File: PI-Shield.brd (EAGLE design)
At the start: 69.8 x 73 mm, 77 parts, among them IC1 PCF8574T, J10 T2I, J11 T2I, J12 T2I, J13 DF13-4P-1.25DSA, J14 DF13-4P-1.25DSA, J15 DF13-4P-1.25DSA, Q1 220mA/50V/3.5Ω, Q2 220mA/50V/3.5Ω, Q3 220mA/50V/3.5Ω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

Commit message: Update PI-Shield.brd
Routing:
- net 5V: track 177.8 -> 182.7 mm, vias 4 -> 5
- net 5V_RAW: track 2.52 -> 6.33 mm
- net SCL: track 141.0 -> 139.3 mm
- net SDA: track 141.7 -> 140.1 mm
- net PI_POWER: track 28.4 -> 30.0 mm
- net SOL6_1: track 47.8 -> 49.2 mm
- net SOL5_1: track 42.0 -> 43.1 mm
- net RESET_MID: track 12.5 -> 13.7 mm
- net SOL4_1: track 37.3 -> 38.3 mm
- net SOL3_1: track 31.8 -> 32.7 mm
- net 3V3: track 219.9 -> 220.7 mm
- net SOL2_1: track 26.9 -> 27.5 mm

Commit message: Added CAN to BKP... Silkscreen as well
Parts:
- removed U$3: 6X_CONN, PI-SHIELD, Solenoid-Backplane:IPL6X2
- added U$9: 7X_CONN, PI-SHIELD, Solenoid-Backplane:IPL7X2
- moved U$6 1.02 mm to (36.7, 5.46)
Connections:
- net 12V: now also U$9.2, U$9.4; no longer U$3.2, U$3.4
- net 3V3: now also U$9.12; no longer U$3.12
- net 5V: now also U$9.8; no longer U$3.8
- net CAN_H: now also U$9.13
- net CAN_L: now also U$9.14
- net GND: now also U$9.10, U$9.6; no longer U$3.10, U$3.6
- net SOL1_1: now also U$9.1; no longer U$3.1
- net SOL2_1: now also U$9.3; no longer U$3.3
- net SOL3_1: now also U$9.5; no longer U$3.5
- net SOL4_1: now also U$9.7; no longer U$3.7
- net SOL5_1: now also U$9.9; no longer U$3.9
- net SOL6_1: now also U$9.11; no longer U$3.11
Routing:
- net CAN_L: track 43.0 -> 137.5 mm, vias 1 -> 2
- net CAN_H: track 43.0 -> 136.6 mm, vias 1 -> 2
- net !AMP_RESET: track 55.6 -> 51.8 mm
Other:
- board text added: "X14 Pi-Shield v1 Rachel Livesay Erin Park Katherine Sandys Read Hedl 1/7/2022"

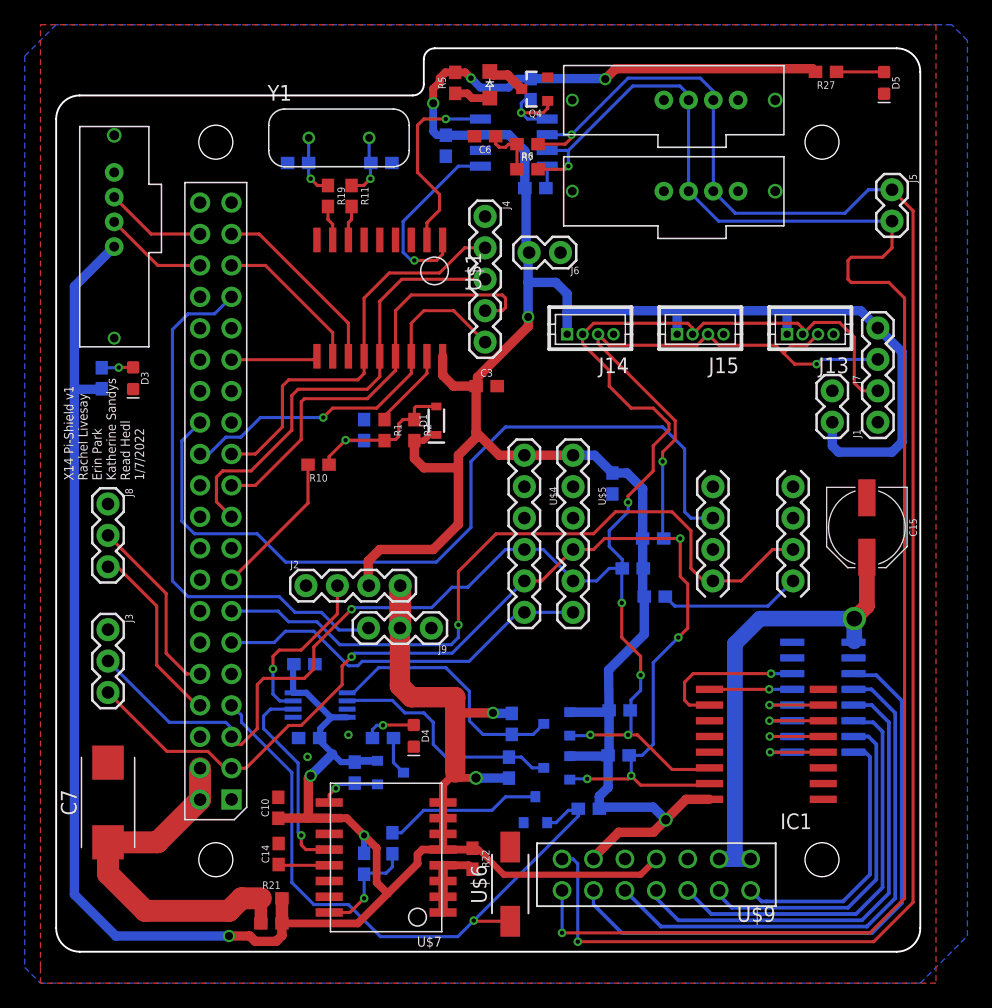
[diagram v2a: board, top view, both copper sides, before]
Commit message: Adjusted Labels
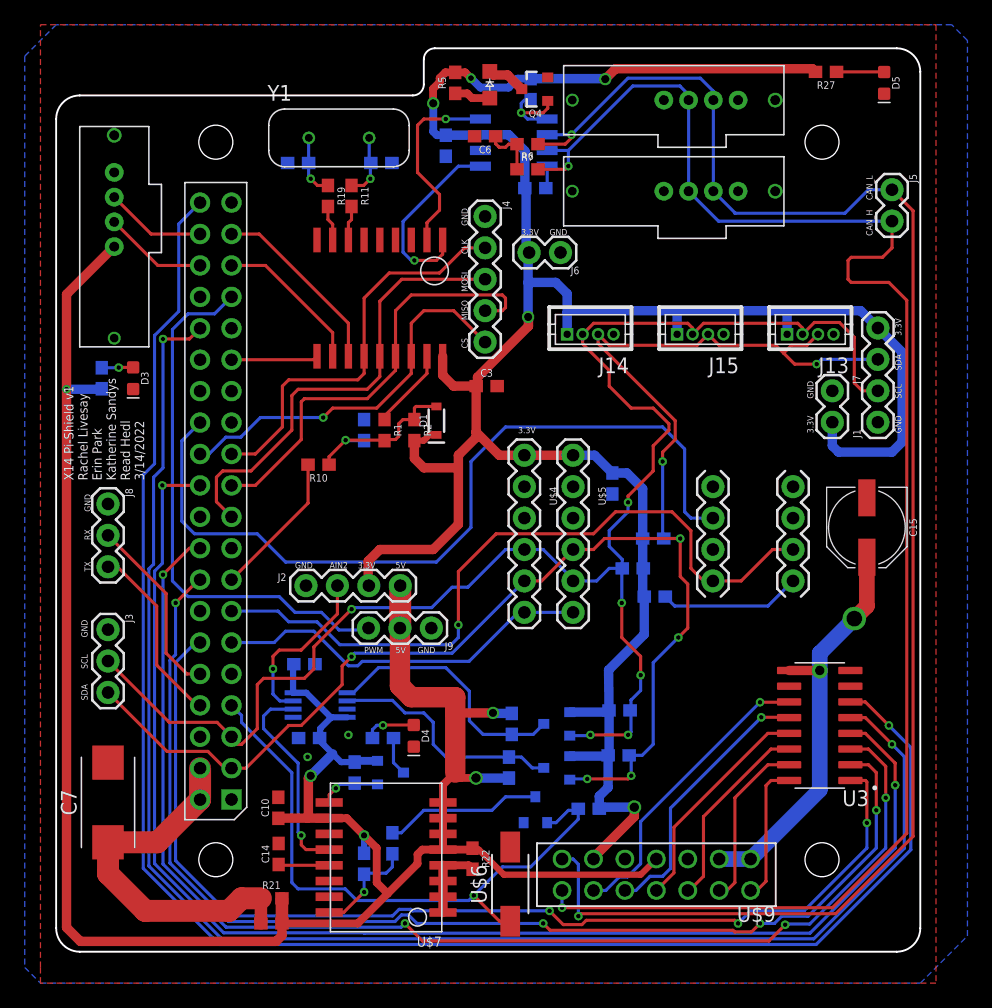
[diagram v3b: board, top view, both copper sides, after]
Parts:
- removed IC1: PCF8574T, micro-philips:SO16W
- moved U3 2.30 mm to (61.7, 18.3), flipped to the top
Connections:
- net 3V3: no longer IC1.16
- net GND: no longer IC1.1, IC1.2, IC1.3, IC1.8
- net GPIO1: now also U$8.12; no longer IC1.4
- net GPIO2: now also U$8.16; no longer IC1.5
- net GPIO3: now also U$8.18; no longer IC1.6
- net GPIO4: now also U$8.22; no longer IC1.7
- net GPIO5: now also U$8.32; no longer IC1.9
- net GPIO6: now also U$8.40; no longer IC1.10
- net SCL: no longer IC1.14
- net SDA: no longer IC1.15
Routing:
- net GPIO6: track 12.6 -> 138.2 mm
- net GPIO5: track 6.70 -> 126.0 mm, vias 1 -> 2
- net GPIO4: track 6.19 -> 110.4 mm, vias 1 -> 2
- net GPIO3: track 6.19 -> 101.7 mm, vias 1 -> 4
- net GPIO2: track 6.14 -> 95.1 mm, vias 1 -> 4
- net GPIO1: track 6.09 -> 86.6 mm, vias 1 -> 3
- net SOL6_1: track 49.2 -> 24.1 mm, vias 0 -> 1
- net SOL5_1: track 43.1 -> 21.9 mm, vias 0 -> 1
- net SOL4_1: track 38.3 -> 18.2 mm
- net SOL3_1: track 32.7 -> 15.8 mm
- net SOL2_1: track 27.5 -> 13.9 mm
- net SOL1_1: track 21.9 -> 11.3 mm
- net 3V3: track 220.7 -> 211.9 mm
- net SCL: track 139.3 -> 131.1 mm
- net SDA: track 140.1 -> 133.4 mm
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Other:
- board text added: "3.3V"
- board text added: "5V"
- board text added: "AIN2"
- board text added: "CAN_H"
- board text added: "CAN_L"
- board text added: "CLK"
- board text added: "CS"
- board text added: "GND"
- board text added: "MISO"
- board text added: "MOSI"
- board text added: "PWM"
- board text added: "RX"
- board text added: "SCL"
- board text added: "SDA"
- board text added: "TX"
- board text added: "X14 Pi-Shield v1 Rachel Livesay Erin Park Katherine Sandys Read Hedl 3/14/2022"
- board text removed: "X14 Pi-Shield v1 Rachel Livesay Erin Park Katherine Sandys Read Hedl 1/7/2022"

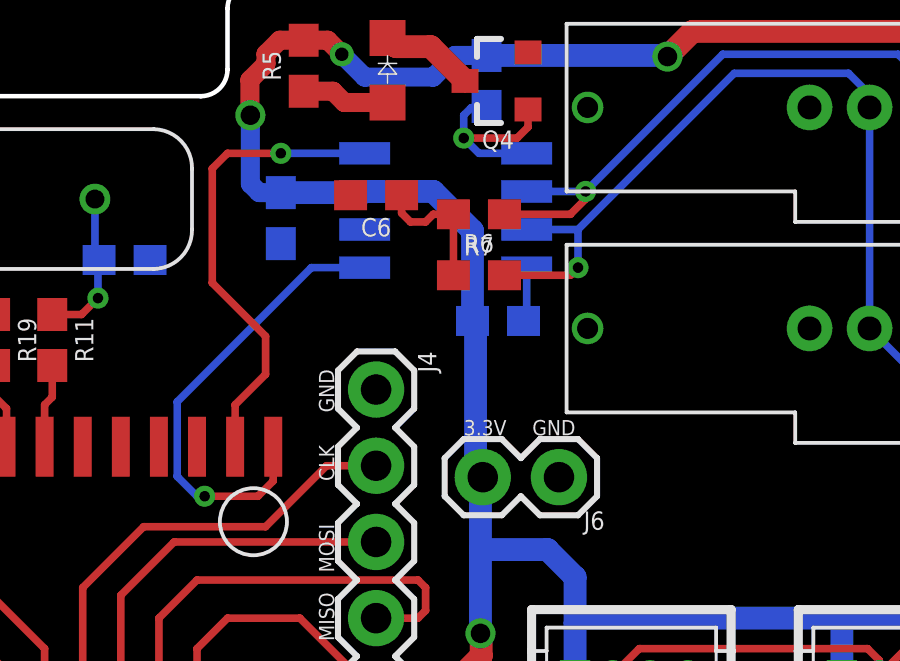
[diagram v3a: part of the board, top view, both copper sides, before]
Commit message: Replaced R3 with Jumper, exported STEP
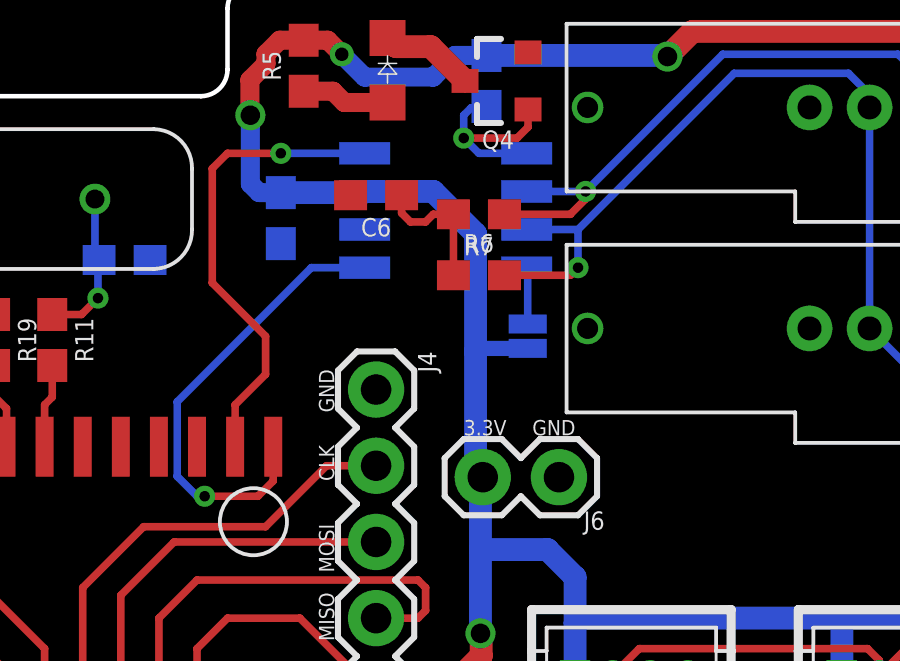
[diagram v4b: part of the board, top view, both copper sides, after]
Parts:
- R3: value (none) -> JUMPER-SMT_2_NO_SILK; device SparkFun-Resistors:0603 -> SparkFun-Jumpers:SMT-JUMPER_2_NO_SILK
- moved R3 1.11 mm to (39.7, 61.2), turned to 270 degrees
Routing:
- net 3V3: track 211.9 -> 213.7 mm
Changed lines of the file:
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@@
 <attribute name="VALUE" x="62.23" y="71.882" size="0.6096" layer="27" font="vector" ratio="20" rot="R180" align="top-center"/>
 </element>
-<element name="R3" library="SparkFun-Resistors" library_urn="urn:adsk.eagle:library:532" package="0603" package3d_urn="urn:adsk.eagle:package:39650/1" value=" " x="38.735" y="61.722" smashed="yes" rot="MR0">
-<attribute name="NAME" x="38.735" y="62.484" size="0.6096" layer="26" font="vector" ratio="20" rot="MR0" align="bottom-center"/>
-<attribute name="PROD_ID" value=" " x="0.635" y="-56.388" size="1.778" layer="28" rot="MR0" display="off"/>
-<attribute name="VALUE" x="38.735" y="60.96" size="0.6096" layer="28" font="vector" ratio="20" rot="MR0" align="top-center"/>
+<element name="R3" library="SparkFun-Jumpers" library_urn="urn:adsk.eagle:library:528" package="SMT-JUMPER_2_NO_SILK" package3d_urn="urn:adsk.eagle:package:39279/1" value="JUMPER-SMT_2_NO_SILK" x="39.7256" y="61.214" smashed="yes" rot="MR270">
+<attribute name="NAME" x="38.9636" y="61.214" size="0.6096" layer="26" font="vector" ratio="20" rot="MR270" align="bottom-center"/>
 </element>
 <element name="R4" library="SparkFun-Resistors" library_urn="urn:adsk.eagle:library:532" package="0603" package3d_urn="urn:adsk.eagle:package:39650/1" value=" " x="38.354" y="69.723" smashed="yes" rot="MR90">
@@
 <wire x1="34.29" y1="66.04" x2="34.251" y2="66.001" width="0.762" layer="16"/>
 <wire x1="34.251" y1="66.001" x2="31.496" y2="66.001" width="0.762" layer="16"/>
-<wire x1="34.29" y1="66.04" x2="36.576" y2="66.04" width="0.762" layer="16"/>
-<wire x1="37.885" y1="64.731" x2="37.885" y2="61.722" width="0.762" layer="16"/>
-<wire x1="36.576" y1="66.04" x2="37.885" y2="64.731" width="0.762" layer="16"/>
+<wire x1="36.576" y1="66.04" x2="34.29" y2="66.04" width="0.762" layer="16"/>
 <wire x1="62.738" y1="42.799" x2="62.738" y2="40.894" width="0.762" layer="16"/>
 <wire x1="62.738" y1="40.894" x2="63.246" y2="40.386" width="0.762" layer="16"/>
@@
 <wire x1="68.3768" y1="41.1988" x2="67.564" y2="40.386" width="0.762" layer="16"/>
 <wire x1="68.3768" y1="48.4632" x2="68.3768" y2="41.1988" width="0.762" layer="16"/>
-<wire x1="37.885" y1="61.722" x2="37.9866" y2="61.6204" width="0.762" layer="16"/>
 <wire x1="25.2222" y1="29.6418" x2="25.273" y2="29.591" width="0.762" layer="1"/>
 <wire x1="30.734" y1="41.776" x2="30.18" y2="41.776" width="0.508" layer="1"/>
@@
 <wire x1="31.242" y1="48.131" x2="31.242" y2="46.607" width="0.762" layer="1"/>
 <wire x1="32.129" y1="45.72" x2="33.948" y2="45.72" width="0.762" layer="1"/>
-<wire x1="37.9866" y1="61.6204" x2="37.9866" y2="56.7554" width="0.762" layer="16"/>
 <wire x1="38.227" y1="56.515" x2="37.9866" y2="56.7554" width="0.762" layer="16"/>
 <wire x1="41.305" y1="49.911" x2="41.305" y2="51.659" width="0.762" layer="16"/>
@@
 <contactref element="U$9" pad="12"/>
 <wire x1="43.434" y1="7.62" x2="43.434" y2="7.493" width="0.762" layer="1"/>
+<wire x1="37.9866" y1="56.7554" x2="37.9866" y2="60.706" width="0.762" layer="16"/>
+<wire x1="37.9866" y1="60.706" x2="37.9866" y2="64.6294" width="0.762" layer="16"/>
+<wire x1="37.9866" y1="64.6294" x2="36.576" y2="66.04" width="0.762" layer="16"/>
+<wire x1="39.7256" y1="60.8076" x2="38.0882" y2="60.8076" width="0.508" layer="16"/>
+<wire x1="38.0882" y1="60.8076" x2="37.9866" y2="60.706" width="0.508" layer="16"/>
 </signal>
 <signal name="FAULT">
@@
 <contactref element="R3" pad="1"/>
 <contactref element="U$2" pad="8"/>
-<wire x1="39.585" y1="61.722" x2="39.69" y2="61.827" width="0.254" layer="16"/>
-<wire x1="39.69" y1="61.827" x2="39.69" y2="63.5" width="0.254" layer="16"/>
+<wire x1="39.7256" y1="61.6204" x2="39.7256" y2="63.4644" width="0.254" layer="16"/>
+<wire x1="39.7256" y1="63.4644" x2="39.69" y2="63.5" width="0.254" layer="16"/>
 </signal>
 <signal name="5V" class="2">
